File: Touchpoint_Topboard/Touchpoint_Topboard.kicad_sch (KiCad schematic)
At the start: 12 parts, among them J1 Conn_01x03, J2 Conn_01x03, J4 EC10E1220501, J5 Conn_01x11, SW3 SW_SPST, U101 AS78L05RTR-E1

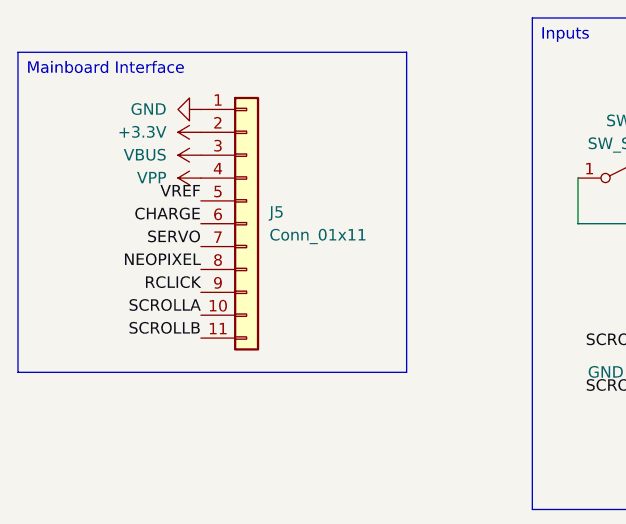
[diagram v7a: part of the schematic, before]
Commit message: Added minor final changes to schematic
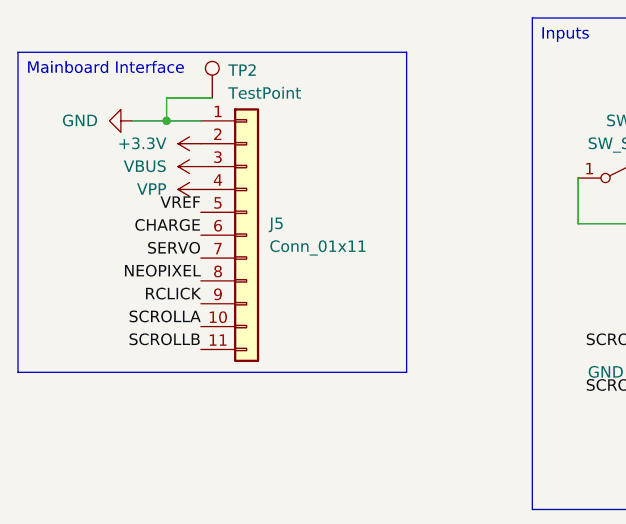
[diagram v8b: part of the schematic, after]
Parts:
- added TP2: TestPoint, TestPoint:TestPoint_Keystone_5019_Miniature, symbol Connector:TestPoint
- J5: footprint (none) -> Touchpoint:Jumper_Interface_11
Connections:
- net GND: now also TP2.1
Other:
- moved on the sheet: J5
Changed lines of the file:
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@@
+	)
+	(junction
+		(at 35.56 30.48)
+		(diameter 0)
+		(color 0 0 0 0)
 	)
 	(junction
@@
 	(wire
 		(pts
-			(xy 81.28 36.83) (xy 81.28 41.91)
+			(xy 35.56 30.48) (xy 35.56 27.94)
 		)
 		(stroke
@@
 	(wire
 		(pts
-			(xy 91.44 36.83) (xy 93.98 36.83)
+			(xy 81.28 36.83) (xy 81.28 41.91)
 		)
 		(stroke
@@
 	(wire
 		(pts
-			(xy 81.28 41.91) (xy 93.98 41.91)
+			(xy 31.75 30.48) (xy 35.56 30.48)
 		)
 		(stroke
@@
 	(wire
 		(pts
-			(xy 93.98 36.83) (xy 99.06 36.83)
+			(xy 91.44 36.83) (xy 93.98 36.83)
 		)
 		(stroke
@@
 	(wire
 		(pts
-			(xy 99.06 36.83) (xy 105.41 36.83)
+			(xy 81.28 41.91) (xy 93.98 41.91)
 		)
 		(stroke
@@
 		)
 	)
+	(wire
+		(pts
+			(xy 93.98 36.83) (xy 99.06 36.83)
+		)
+		(stroke
+			(width 0)
+			(type default)
+		)
+	)
+	(wire
+		(pts
+			(xy 35.56 27.94) (xy 40.64 27.94)
+		)
+		(stroke
+			(width 0)
+			(type default)
+		)
+	)
+	(wire
+		(pts
+			(xy 35.56 30.48) (xy 39.37 30.48)
+		)
+		(stroke
+			(width 0)
+			(type default)
+		)
+	)
+	(wire
+		(pts
+			(xy 99.06 36.83) (xy 105.41 36.83)
+		)
+		(stroke
+			(width 0)
+			(type default)
+		)
+	)
 	(label "SERVO"
-		(at 39.37 44.45 180)
+		(at 39.37 45.72 180)
 		(effects
 			(font
@@
 	)
 	(label "CHARGE"
-		(at 39.37 41.91 180)
+		(at 39.37 43.18 180)
 		(effects
 			(font
@@
 	)
 	(label "NEOPIXEL"
-		(at 39.37 46.99 180)
+		(at 39.37 48.26 180)
 		(effects
 			(font
@@
 	)
 	(label "SCROLLA"
-		(at 39.37 52.07 180)
+		(at 39.37 53.34 180)
 		(effects
 			(font
@@
 	)
 	(label "SCROLLB"
-		(at 39.37 54.61 180)
+		(at 39.37 55.88 180)
 		(effects
 			(font
@@
 	)
 	(label "RCLICK"
-		(at 39.37 49.53 180)
+		(at 39.37 50.8 180)
 		(effects
 			(font
@@
 	)
 	(label "VREF"
-		(at 39.37 39.37 180)
+		(at 39.37 40.64 180)
 		(effects
 			(font
@@
 	(symbol
 		(lib_id "Connector_Generic:Conn_01x11")
-		(at 44.45 41.91 0)
+		(at 44.45 43.18 0)
 		(unit 1)
 		(exclude_from_sim no)
@@
 		(fields_autoplaced yes)
 		(property "Reference" "J5"
-			(at 46.99 40.6399 0)
+			(at 46.99 41.9099 0)
 			(effects
 				(font
@@
 		)
 		(property "Value" "Conn_01x11"
-			(at 46.99 43.1799 0)
-			(effects
-				(font
-					(size 1.27 1.27)
-				)
-				(justify left)
-			)
-		)
-		(property "Footprint" ""
-			(at 44.45 41.91 0)
+			(at 46.99 44.4499 0)
+			(effects
+				(font
+					(size 1.27 1.27)
+				)
+				(justify left)
+			)
+		)
+		(property "Footprint" "Touchpoint:Jumper_Interface_11"
+			(at 44.45 43.18 0)
 			(effects
 				(font
@@
 		)
 		(property "Datasheet" "~"
-			(at 44.45 41.91 0)
+			(at 44.45 43.18 0)
 			(effects
 				(font
@@
 		)
 		(property "Description" "Generic connector, single row, 01x11, script generated (kicad-library-utils/schlib/autogen/connector/)"
-			(at 44.45 41.91 0)
+			(at 44.45 43.18 0)
 			(effects
 				(font
@@
 	(symbol
 		(lib_id "power:VBUS")
-		(at 39.37 34.29 90)
+		(at 39.37 35.56 90)
 		(unit 1)
 		(exclude_from_sim no)
@@
 		(fields_autoplaced yes)
 		(property "Reference" "#PWR019"
-			(at 43.18 34.29 0)
+			(at 43.18 35.56 0)
 			(effects
 				(font
@@
 		)
 		(property "Value" "VBUS"
-			(at 35.56 34.2899 90)
+			(at 35.56 35.5599 90)
 			(effects
 				(font
@@
 		)
 		(property "Footprint" ""
-			(at 39.37 34.29 0)
+			(at 39.37 35.56 0)
 			(effects
 				(font
@@
 		)
 		(property "Datasheet" ""
-			(at 39.37 34.29 0)
+			(at 39.37 35.56 0)
 			(effects
 				(font
@@
 		)
 		(property "Description" "Power symbol creates a global label with name \"VBUS\""
-			(at 39.37 34.29 0)
+			(at 39.37 35.56 0)
 			(effects
 				(font
@@
 	)
 	(symbol
+		(lib_id "Connector:TestPoint")
+		(at 40.64 27.94 0)
+		(unit 1)
+		(exclude_from_sim no)
+		(in_bom yes)
+		(on_board yes)
+		(dnp no)
+		(property "Reference" "TP2"
+			(at 42.418 24.892 0)
+			(effects
+				(font
+					(size 1.27 1.27)
+				)
+				(justify left)
+			)
+		)
+		(property "Value" "TestPoint"
+			(at 42.418 27.432 0)
+			(effects
+				(font
+					(size 1.27 1.27)
+				)
+				(justify left)
+			)
+		)
+		(property "Footprint" "TestPoint:TestPoint_Keystone_5019_Miniature"
+			(at 45.72 27.94 0)
+			(effects
+				(font
+					(size 1.27 1.27)
+				)
+				(hide yes)
+			)
+		)
+		(property "Datasheet" "~"
+			(at 45.72 27.94 0)
+			(effects
+				(font
+					(size 1.27 1.27)
+				)
+				(hide yes)
+			)
+		)
+		(property "Description" "test point"
+			(at 40.64 27.94 0)
+			(effects
+				(font
+					(size 1.27 1.27)
+				)
+				(hide yes)
+			)
+		)
+		(pin "1"
+		)
+		(instances
+			(project ""
+				(path "/7efcba5d-f3d7-4197-a753-e42cd4117b88"
+					(reference "TP2")
+					(unit 1)
+				)
+			)
+		)
+	)
+	(symbol
 		(lib_id "Connector_Generic:Conn_01x03")
 		(at 149.86 29.21 0)
@@
 	(symbol
 		(lib_id "power:GND")
-		(at 39.37 29.21 270)
+		(at 31.75 30.48 270)
 		(unit 1)
 		(exclude_from_sim no)
@@
 		(fields_autoplaced yes)
 		(property "Reference" "#PWR018"
-			(at 33.02 29.21 0)
+			(at 25.4 30.48 0)
 			(effects
 				(font
@@
 		)
 		(property "Value" "GND"
-			(at 35.56 29.2099 90)
+			(at 27.94 30.4799 90)
 			(effects
 				(font
@@
 		)
 		(property "Footprint" ""
-			(at 39.37 29.21 0)
+			(at 31.75 30.48 0)
 			(effects
 				(font
@@
 		)
 		(property "Datasheet" ""
-			(at 39.37 29.21 0)
+			(at 31.75 30.48 0)
 			(effects
 				(font
@@
 		)
 		(property "Description" "Power symbol creates a global label with name \"GND\" , ground"
-			(at 39.37 29.21 0)
+			(at 31.75 30.48 0)
 			(effects
 				(font
@@
 	(symbol
 		(lib_id "power:VBUS")
-		(at 39.37 31.75 90)
+		(at 39.37 33.02 90)
 		(unit 1)
 		(exclude_from_sim no)
@@
 		(fields_autoplaced yes)
 		(property "Reference" "#PWR021"
-			(at 43.18 31.75 0)
+			(at 43.18 33.02 0)
 			(effects
 				(font
@@
 		)
 		(property "Value" "+3.3V"
-			(at 35.56 31.7499 90)
+			(at 35.56 33.0199 90)
 			(effects
 				(font
@@
 		)
 		(property "Footprint" ""
-			(at 39.37 31.75 0)
+			(at 39.37 33.02 0)
 			(effects
 				(font
@@
 		)
 		(property "Datasheet" ""
-			(at 39.37 31.75 0)
+			(at 39.37 33.02 0)
 			(effects
 				(font
@@
 		)
 		(property "Description" "Power symbol creates a global label with name \"VBUS\""
-			(at 39.37 31.75 0)
+			(at 39.37 33.02 0)
 			(effects
 				(font
@@
 	(symbol
 		(lib_id "power:VPP")
-		(at 39.37 36.83 90)
+		(at 39.37 38.1 90)
 		(unit 1)
 		(exclude_from_sim no)
@@
 		(dnp no)
 		(property "Reference" "#PWR020"
-			(at 43.18 36.83 0)
+			(at 43.18 38.1 0)
 			(effects
 				(font
@@
 		)
 		(property "Value" "VPP"
-			(at 35.56 36.8299 90)
+			(at 35.56 38.0999 90)
 			(effects
 				(font
@@
 		)
 		(property "Footprint" ""
-			(at 39.37 36.83 0)
+			(at 39.37 38.1 0)
 			(effects
 				(font
@@
 		)
 		(property "Datasheet" ""
-			(at 39.37 36.83 0)
+			(at 39.37 38.1 0)
 			(effects
 				(font
@@
 		)
 		(property "Description" "Power symbol creates a global label with name \"VPP\""
-			(at 39.37 36.83 0)
-			(effects
-				(font
+			(at 39.37 38.1 0)
+			(effects
+				(font
